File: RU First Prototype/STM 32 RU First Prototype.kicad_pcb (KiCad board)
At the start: 4 copper layers, 99 parts, among them J1 Conn_01x02, J10 Conn_01x02_Pin, J11 Conn_01x02_Pin, J12 1776113-2, J2 USB_C_Receptacle, J3 Conn_01x02_Pin, J4 Conn_01x04, J5 Conn_01x02_Pin, J6 1776113-2, J7 1776113-2, J8 1776113-2, J9 Conn_01x02_Pin, Q1 SISA96DN-T1, Q2 SISA96DN-T1, Q3 SISA96DN-T1, Q4 SISA96DN-T1, SW1 SW_SPDT, U1 STM32F412RGTx, U2 AMS1117-3.3, U3 MS5611, U4 KX134-1211, U5 W25Q16JVSS, U6 TCAN330, U7 TCAN330, Y1 Crystal_8Mhz

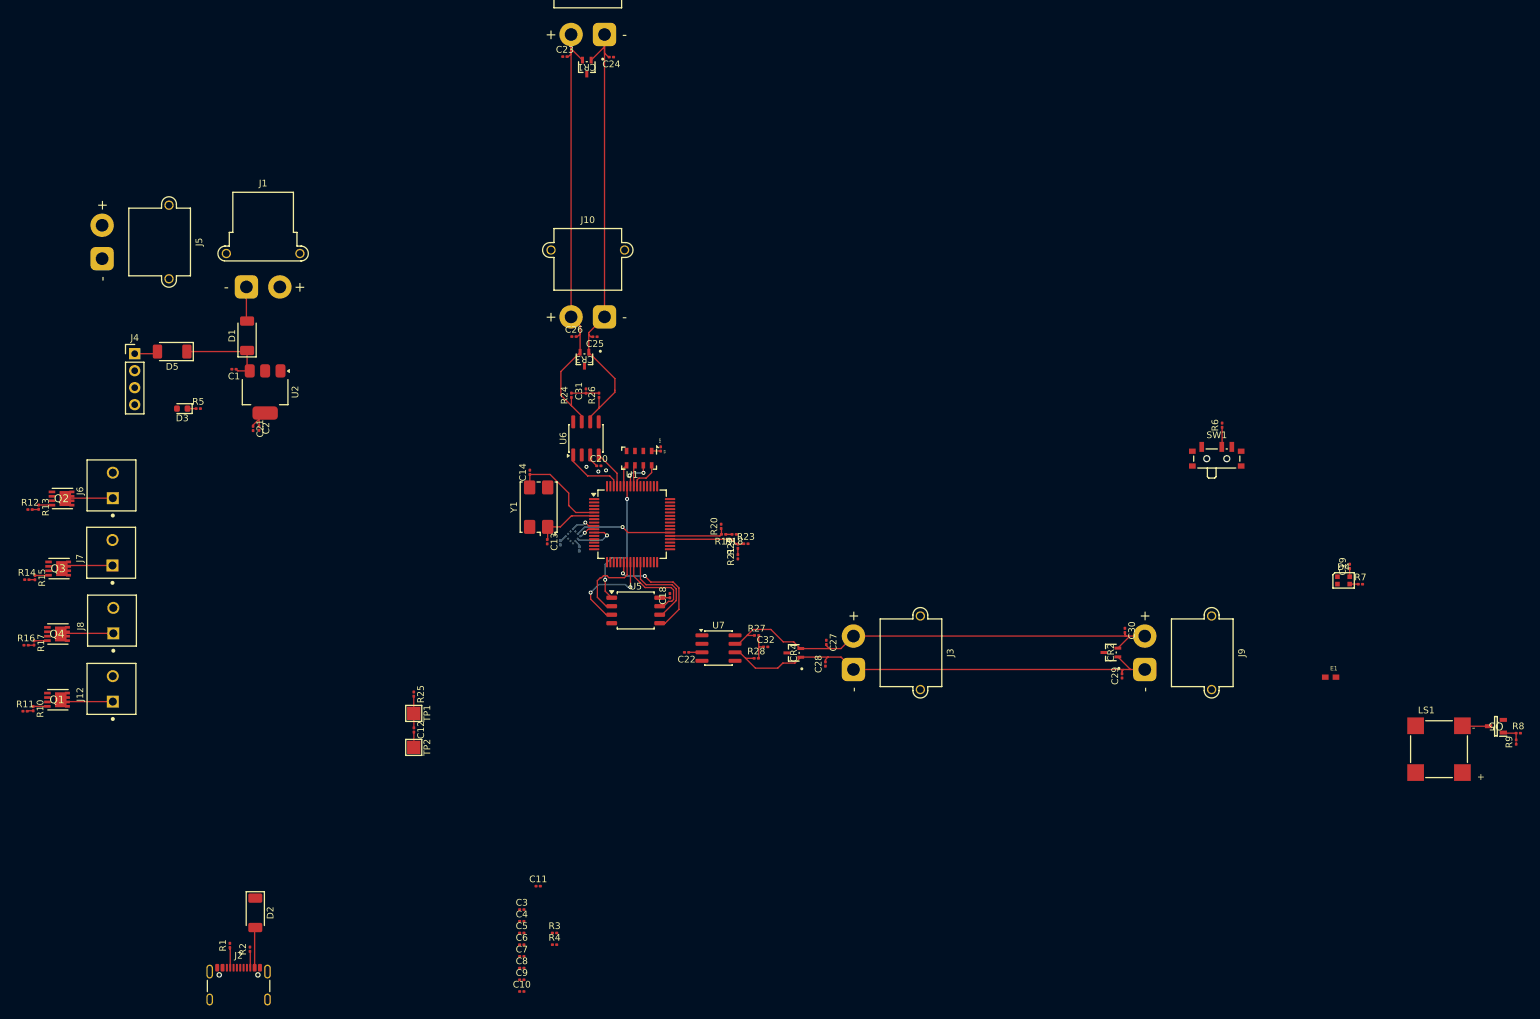
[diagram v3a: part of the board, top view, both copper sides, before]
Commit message: Added some more traces
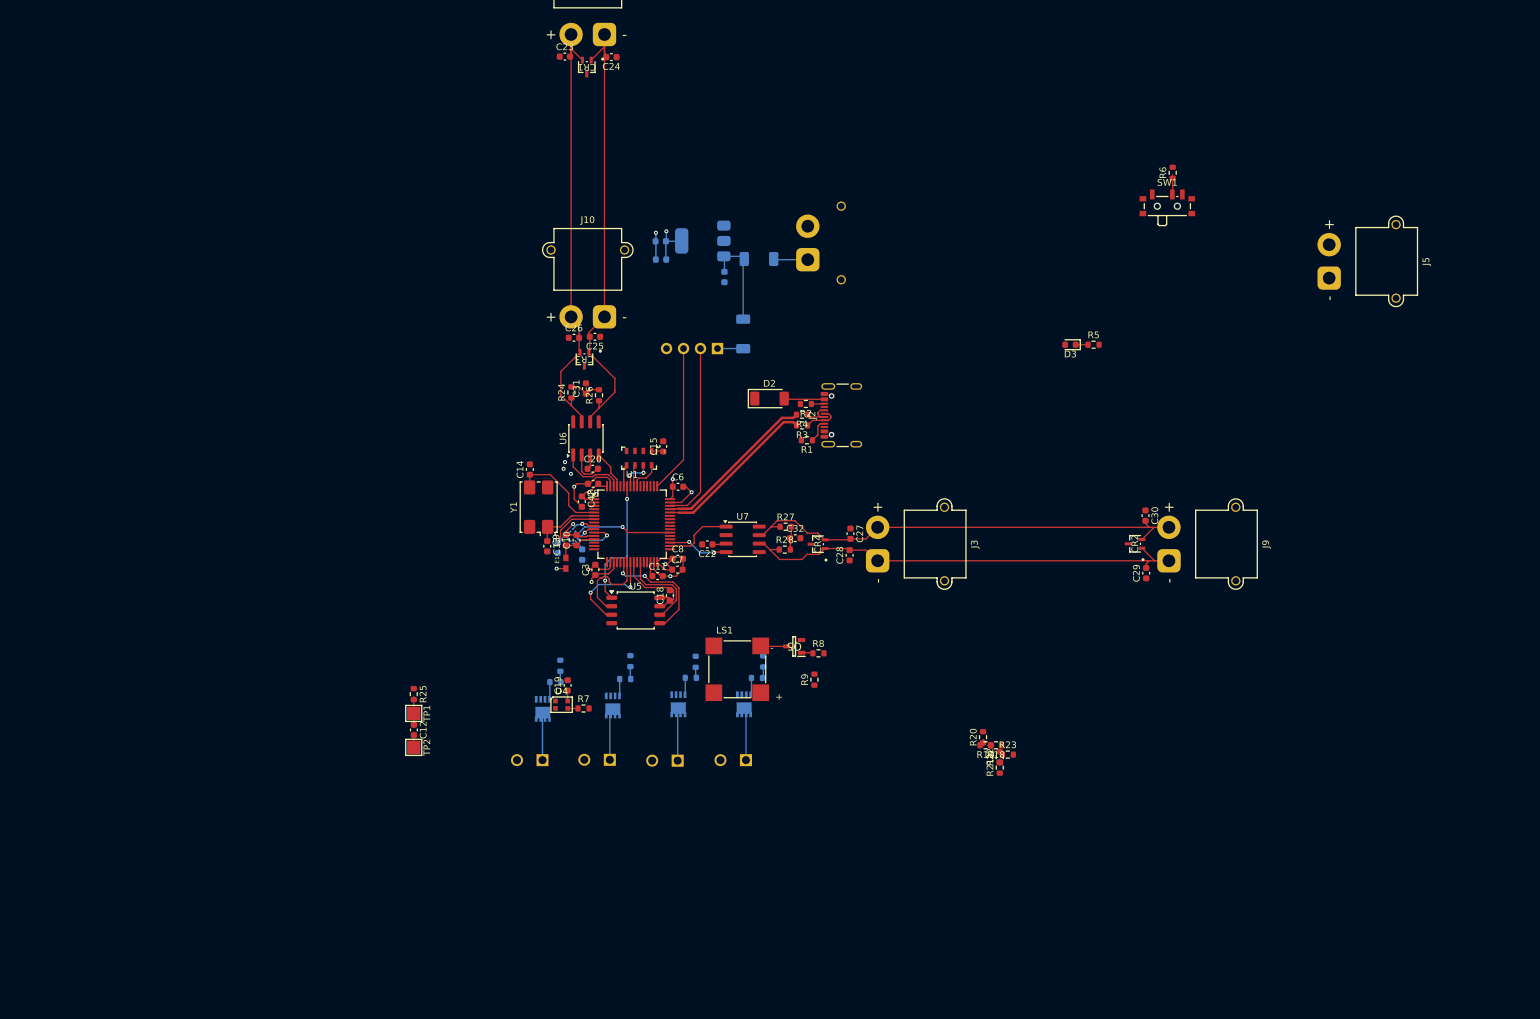
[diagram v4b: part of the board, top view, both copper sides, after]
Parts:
- C1, C2, C21: footprint Capacitor_SMD:C_0201_0603Metric -> Capacitor_SMD:C_0603_1608Metric; moved to B.Cu
- C10, C11, C12, C13, C14, C15, C16, C17, C18, C19, C20, C22, C23, C24, C25, C26, C27, C28, C29, C3, C30, C31, C32, C4, C5, C6, C7, C8, C9: footprint Capacitor_SMD:C_0201_0603Metric -> Capacitor_SMD:C_0603_1608Metric
- D1, D5, J1, J12, J4, J6, J7, J8, Q1, Q2, Q3, Q4, U2: moved to B.Cu
- R1, R18, R19, R2, R20, R21, R22, R23, R24, R25, R26, R27, R28, R3, R4, R5, R6, R7, R8, R9: footprint Resistor_SMD:R_0201_0603Metric -> Resistor_SMD:R_0603_1608Metric
- R10, R11, R12, R13, R14, R15, R16, R17: footprint Resistor_SMD:R_0201_0603Metric -> Resistor_SMD:R_0603_1608Metric; moved to B.Cu
- moved J5 183.5 mm to (225.6, 63.0)
- moved R5 134.2 mm to (190.4, 73.0)
- moved D3 133.1 mm to (186.9, 73.0)
- moved J2 125.6 mm to (153.8, 83.5), turned to 90 degrees
- moved D4 118.4 mm to (110.8, 126.8)
- moved C19 118.3 mm to (111.7, 123.9)
- moved R7 117.6 mm to (114.1, 127.4)
- moved R2 116.4 mm to (147.4, 81.8), turned to 180 degrees
- moved E1 115.6 mm to (111.5, 105.6), turned to 90 degrees
- moved R1 114.7 mm to (147.5, 87.2), turned to 180 degrees
- moved R11 110.6 mm to (141.0, 120.3), turned to -90 degrees
- moved D2 108.7 mm to (141.9, 81.0), turned to 0 degrees
- moved R10 108.3 mm to (140.0, 122.8), turned to 0 degrees
- moved LS1 105.6 mm to (137.1, 121.5)
- moved Q5 105.6 mm to (145.6, 118.1)
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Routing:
- net GND: track 2.31 -> 47.8 mm, vias 0 -> 6
- net +3V3: track 15.3 -> 44.2 mm, vias 0 -> 6
- net /SWDIO: track 0.00 -> 26.9 mm
- net /D+: track 0.00 -> 24.8 mm
- net /D-: track 0.00 -> 24.7 mm
- net /SWCLK: track 0.00 -> 22.3 mm
- net /PB15: track 11.3 -> 0.00 mm
- net /CAN_TX2: track 0.00 -> 10.3 mm
- net /CAN_RX2: track 0.00 -> 9.15 mm, vias 0 -> 2
- net /PC6: track 8.68 -> 1.22 mm
- net /NRST: track 4.73 -> 11.7 mm
- net Net-(U1-VDDA): track 0.00 -> 6.56 mm
- net Net-(J2-D--PadA7): track 0.00 -> 5.35 mm
- net Net-(J2-D+-PadA6): track 0.00 -> 5.19 mm
- net Net-(U1-VCAP_1): track 0.00 -> 2.21 mm
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
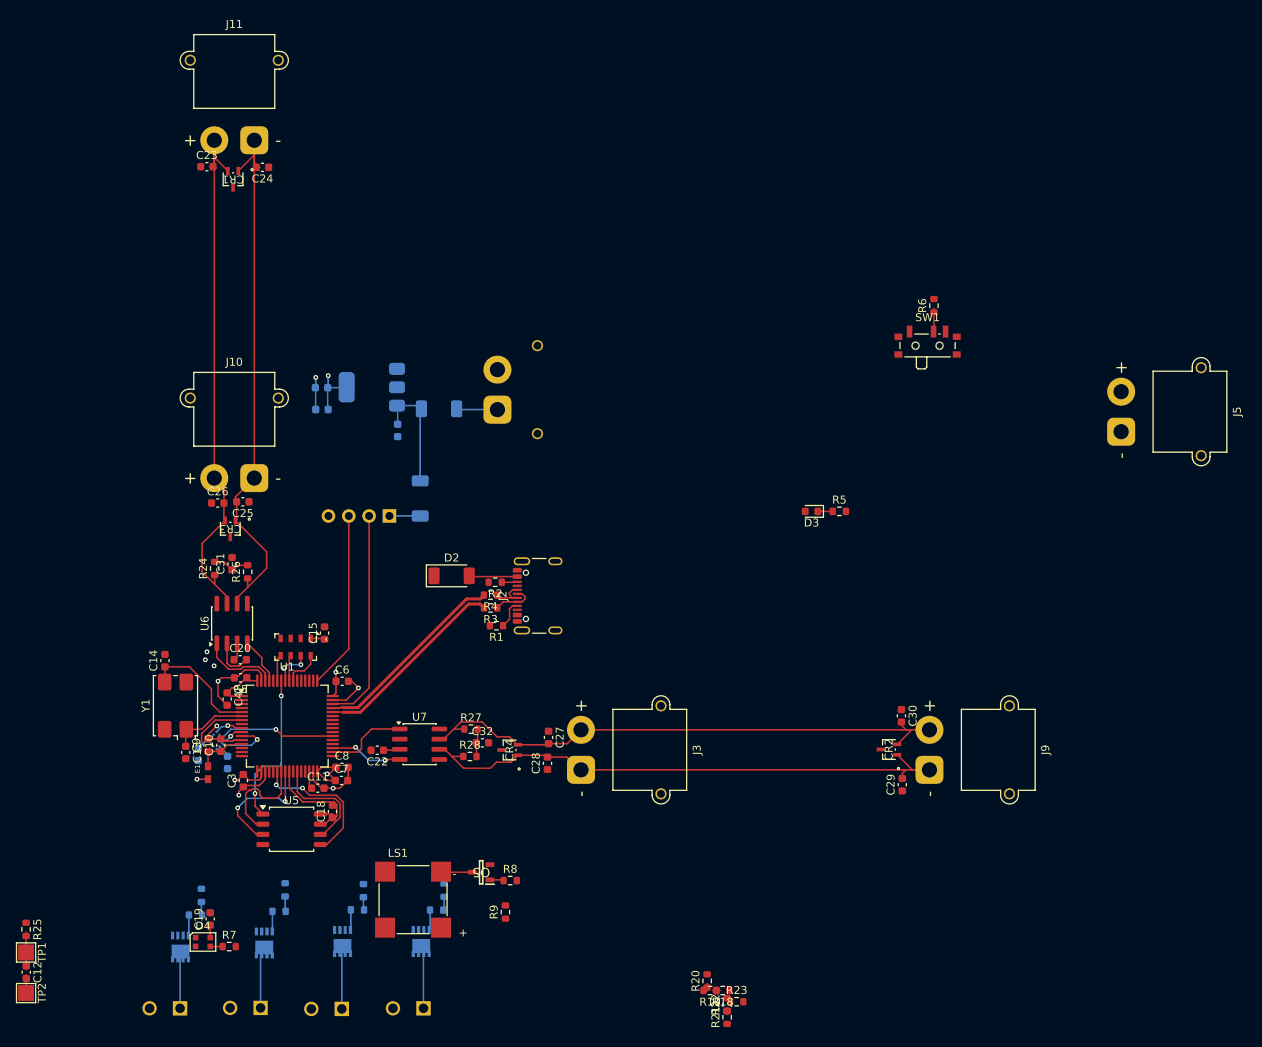
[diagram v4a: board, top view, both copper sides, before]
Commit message: Changing XT30 connectors left
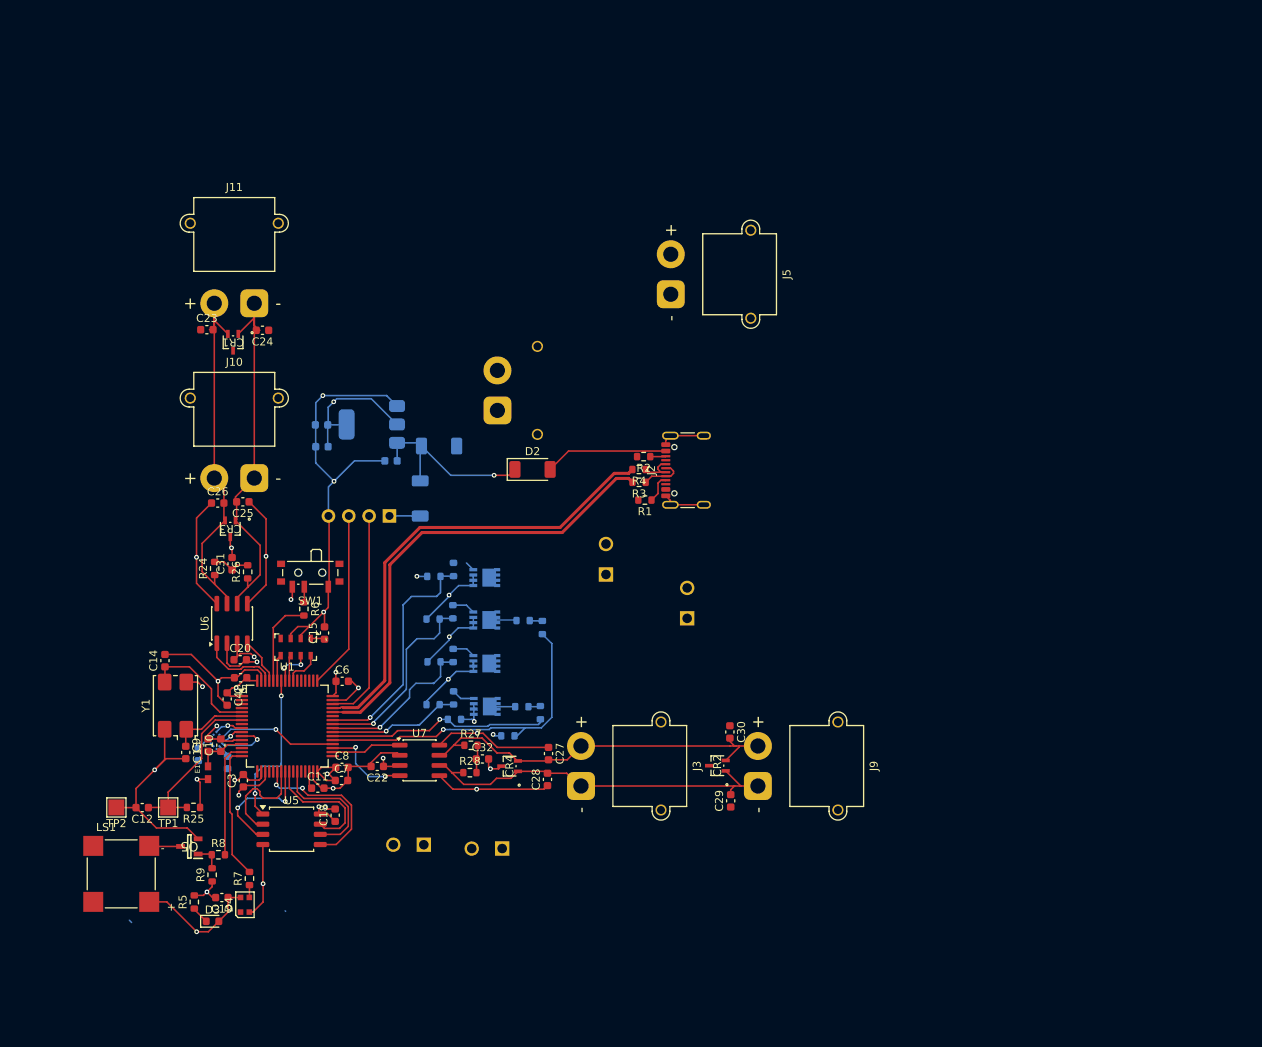
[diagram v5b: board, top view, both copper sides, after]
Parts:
- R18, R19, R20, R21, R22, R23: moved to B.Cu
- moved R5 94.3 mm to (109.8, 121.8), turned to 90 degrees
- moved D3 90.7 mm to (112.0, 124.2), turned to 0 degrees
- moved R6 87.4 mm to (123.5, 85.2), turned to -90 degrees
- moved SW1 82.4 mm to (124.2, 81.0), turned to 180 degrees
- moved J6 78.7 mm to (161.2, 78.9), turned to 90 degrees
- moved J12 61.5 mm to (171.4, 84.4), turned to 90 degrees
- moved Q2 60.0 mm to (146.2, 81.2), turned to 0 degrees
- moved J5 58.9 mm to (169.3, 45.8)
- moved R13 53.9 mm to (142.2, 80.2), turned to -90 degrees
- moved R18 52.5 mm to (150.8, 86.6), turned to 0 degrees
- moved R19 50.0 mm to (153.3, 87.5), turned to -90 degrees
- moved R23 49.9 mm to (142.3, 99.0)
- moved R12 49.3 mm to (139.7, 81.1), turned to 0 degrees
- moved R21 46.5 mm to (150.7, 97.4), turned to 0 degrees
- moved R22 43.3 mm to (153.0, 98.1), turned to -90 degrees
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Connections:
- U1 pad 16: unconnected-(U1-PA2-Pad16) -> /mLED
- U1 pad 36: /PB15 -> /KX_SCK
- U1 pad 38: /KX_SCK -> /PB15
- U1 pad 39: unconnected-(U1-PC8-Pad39) -> /Drogue
- U1 pad 40: /mLED -> /Drogue2
- U1 pad 43: /Drogue -> unconnected-(U1-PA10-Pad43)
- U1 pad 51: /Drogue2 -> unconnected-(U1-PC10-Pad51)
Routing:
- net GND: track 47.8 -> 269.0 mm, vias 6 -> 26
- net /PC6: track 1.22 -> 41.3 mm, vias 0 -> 1
- net +3V3: track 44.2 -> 80.1 mm, vias 6 -> 11
- net /D+: track 24.8 -> 58.5 mm
- net /D-: track 24.7 -> 58.4 mm
- net /PB15: track 0.00 -> 27.9 mm, vias 0 -> 1
- net /Main2: track 1.66 -> 29.6 mm, vias 0 -> 1
- net /Main: track 1.70 -> 24.6 mm, vias 0 -> 1
- net /CAN_L2: track 69.7 -> 48.2 mm
- net /CAN_H2: track 69.2 -> 47.7 mm
- net /CAN_L: track 68.4 -> 48.8 mm
- net /Drogue2: track 1.61 -> 20.7 mm, vias 0 -> 1
- net /CAN_H: track 66.6 -> 47.8 mm
- net /mLED: track 0.00 -> 16.8 mm
- net /Drogue: track 1.88 -> 17.1 mm, vias 0 -> 1
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
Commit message: Routing Round One done
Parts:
- J1: footprint Connector_AMASS:AMASS_XT30PW-F_1x02_P2.50mm_Horizontal -> Connector_AMASS:AMASS_XT30U-M_1x02_P5.0mm_Vertical
- J10, J11, J3, J5, J9: footprint Connector_AMASS:AMASS_XT30PW-M_1x02_P2.50mm_Horizontal -> Connector_AMASS:AMASS_XT30UPB-M_1x02_P5.0mm_Vertical
- moved J7 46.1 mm to (181.4, 104.2), turned to 90 degrees
- moved J8 40.1 mm to (181.4, 95.8), turned to 90 degrees
- moved J6 20.2 mm to (181.4, 78.9)
- moved J5 18.8 mm to (184.1, 57.5), turned to 180 degrees
- moved J12 10.5 mm to (181.4, 87.3)
- moved C29 9.89 mm to (166.9, 109.1)
- moved C30 9.88 mm to (166.8, 100.5)
- moved CR2 9.88 mm to (165.3, 104.7)
- moved C24 9.85 mm to (118.3, 60.2)
- moved C23 9.85 mm to (111.3, 60.1)
- moved CR1 9.85 mm to (114.6, 61.7)
- moved J11 8.92 mm to (117.8, 55.9), turned to 180 degrees
- moved J9 8.23 mm to (172.0, 107.3), turned to 90 degrees
- moved J1 6.12 mm to (142.2, 57.5), turned to 0 degrees
- moved J10 1.90 mm to (117.3, 66.9), turned to 180 degrees
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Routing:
- net /V_PYRO: track 0.00 -> 71.0 mm
- net /V_2S: track 0.28 -> 47.7 mm
- net /V_DROGUE: track 3.20 -> 42.7 mm, vias 0 -> 1
- net /V_MAIN: track 3.83 -> 41.2 mm
- net /V_DROGUE2: track 0.13 -> 37.3 mm, vias 0 -> 1
- net /V_MAIN2: track 0.00 -> 35.0 mm
- net /CAN_L: track 48.8 -> 36.8 mm
- net /CAN_H: track 47.8 -> 35.9 mm
- net /CAN_L2: track 48.2 -> 40.6 mm
- net /CAN_H2: track 47.7 -> 40.4 mm
- net GND: track 269.0 -> 274.4 mm, vias 26 -> 27

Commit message: Update
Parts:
- J10, J11, J3, J5, J9: footprint Connector_AMASS:AMASS_XT30UPB-M_1x02_P5.0mm_Vertical -> Connector_AMASS:AMASS_XT30U-M_1x02_P5.0mm_Vertical
- moved J5 84.9 mm to (99.8, 67.6), turned to 90 degrees
- moved J12 82.3 mm to (99.2, 83.7)
- moved J6 82.3 mm to (99.2, 75.3)
- moved J7 82.3 mm to (99.2, 100.6)
- moved J8 82.3 mm to (99.2, 92.1)
- moved J9 45.2 mm to (134.2, 132.2), turned to 0 degrees
- moved C29 38.7 mm to (133.0, 127.7), turned to 0 degrees
- moved C30 38.0 mm to (140.4, 127.8), turned to 180 degrees
- moved J2 37.1 mm to (143.8, 91.5)
- moved R1 37.1 mm to (137.6, 95.3)
- moved R2 37.1 mm to (137.4, 89.8)
- moved R3 37.1 mm to (136.8, 93.1)
- moved R4 37.1 mm to (136.8, 91.5)
- moved CR2 35.5 mm to (136.8, 126.1), turned to 0 degrees
- moved J3 29.0 mm to (134.2, 120.7), turned to 0 degrees
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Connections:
- R19 pad 2: /PC6 -> /PC7
- R20 pad 1: /PC6 -> /PC7
- R22 pad 2: /PB15 -> /PC6
- R23 pad 1: /PB15 -> /PC6
- U1 pad 38: /PB15 -> /PC7
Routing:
- net GND: track 274.4 -> 11.4 mm, vias 27 -> 0
- net /D+: track 58.5 -> 12.7 mm
- net /D-: track 58.4 -> 12.6 mm
- net /PC6: track 41.3 -> 9.99 mm
- net /PB15: track 27.9 -> 0.00 mm, vias 1 -> 0
- net /V_PYRO: track 71.0 -> 47.1 mm
- net /Drogue2: track 20.7 -> 4.56 mm
- net /PC7: track 0.00 -> 13.5 mm, vias 0 -> 1
- net /V_DROGUE2: track 37.3 -> 24.1 mm, vias 1 -> 0
- net /Main2: track 29.6 -> 18.9 mm
- net /V_MAIN: track 41.2 -> 32.1 mm
- net /V_MAIN2: track 35.0 -> 27.1 mm
- net /CAN_L2: track 40.6 -> 32.7 mm
- net /V_DROGUE: track 42.7 -> 35.1 mm, vias 1 -> 0
- net /CAN_H2: track 40.4 -> 33.0 mm
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
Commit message: Compactness ++
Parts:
- removed J6, J8: 1776113-2, 1776113-2:TE_1776113-2
- removed Q2, Q4: SISA96DN-T1, SISA96DN-T1:SIS862DNT1GE3
- removed R12, R16: 10k, Resistor_SMD:R_0603_1608Metric
- removed R13, R17: 100, Resistor_SMD:R_0603_1608Metric
- moved D3 67.7 mm to (132.9, 59.6), turned to -90 degrees
- moved R5 66.5 mm to (135.5, 58.9), turned to 0 degrees
- moved C21 20.5 mm to (115.2, 82.4)
- moved U2 20.5 mm to (121.5, 79.7)
- moved C1 20.5 mm to (123.8, 84.2)
- moved C2 20.5 mm to (115.2, 79.7)
- moved J9 17.0 mm to (122.4, 119.9), turned to -90 degrees
- moved J7 16.8 mm to (106.2, 85.3)
- moved C30 13.8 mm to (126.8, 126.2), turned to 90 degrees
- moved LS1 11.8 mm to (111.7, 123.0), turned to 90 degrees
- moved C29 10.9 mm to (126.9, 118.7), turned to -90 degrees
- moved J12 9.99 mm to (106.1, 76.5)
- moved CR2 8.98 mm to (128.5, 122.5), turned to -90 degrees
- moved SW1 8.82 mm to (126.3, 72.4)
- moved D2 8.52 mm to (135.6, 85.5)
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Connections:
- U1 pad 40: /Drogue2 -> unconnected-(U1-PC9-Pad40)
- U1 pad 42: /Main2 -> unconnected-(U1-PA9-Pad42)
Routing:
- net /V_PYRO: track 47.1 -> 18.6 mm
- net /V_MAIN2: track 27.1 -> 0.56 mm
- net /V_DROGUE2: track 24.1 -> 0.00 mm
- net /Main2: track 18.9 -> 0.00 mm, vias 1 -> 0
- net /V_IN: track 22.1 -> 39.9 mm
- net /V_USB: track 11.1 -> 0.42 mm
- net /V_2S: track 54.1 -> 43.9 mm
- net Net-(SW1-B): track 2.05 -> 11.4 mm
- net /CAN_H2: track 33.0 -> 40.1 mm
- net Net-(Q5-D): track 3.74 -> 9.88 mm
- net /V_DROGUE: track 35.1 -> 29.1 mm
- net /Drogue2: track 4.56 -> 0.00 mm, vias 1 -> 0
- net /mLED: track 14.3 -> 9.73 mm
- net GND: track 11.4 -> 6.88 mm
- net /Buzzer_G: track 11.9 -> 7.59 mm
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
